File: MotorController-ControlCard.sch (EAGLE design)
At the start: 47 parts, among them J1 SL07-HORIZ, J2 SL03THROUGH_HOLE, Q7 MOSFET-PCHANNEL, Q8 MOSFET-PCHANNEL, U1 TMS320F28069MPZT, U2 MAX3232D, U3 TMS320F28069MPZT

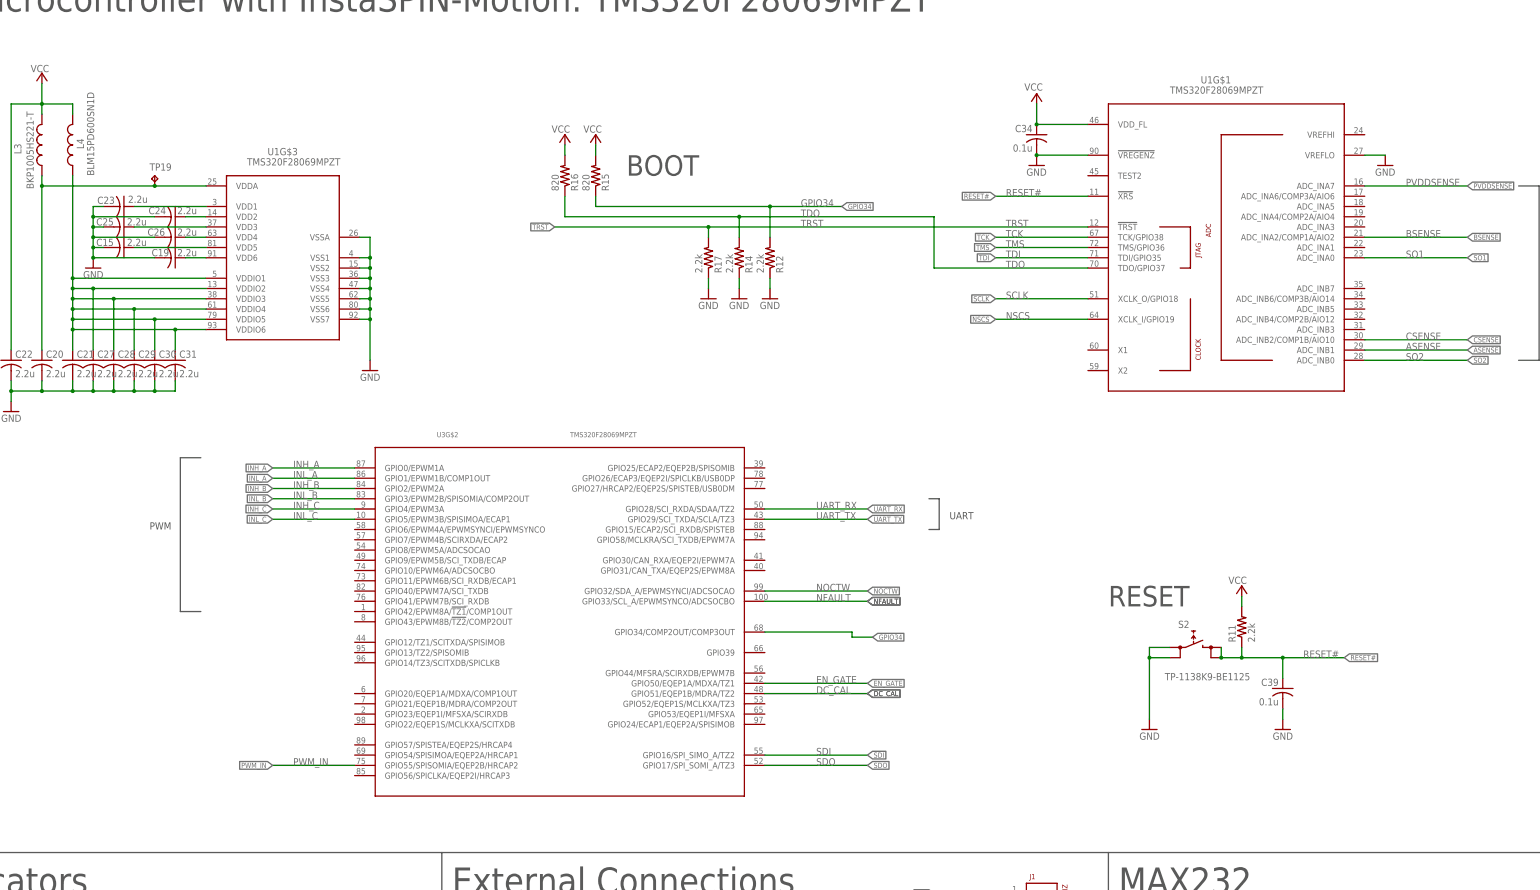
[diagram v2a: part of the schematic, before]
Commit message: Fixed Double tiva chip
Had to copy in a new set of the Tiva chip components from the Original schematic  and then I copied over all schematic routing.  New layout started due to this setback.
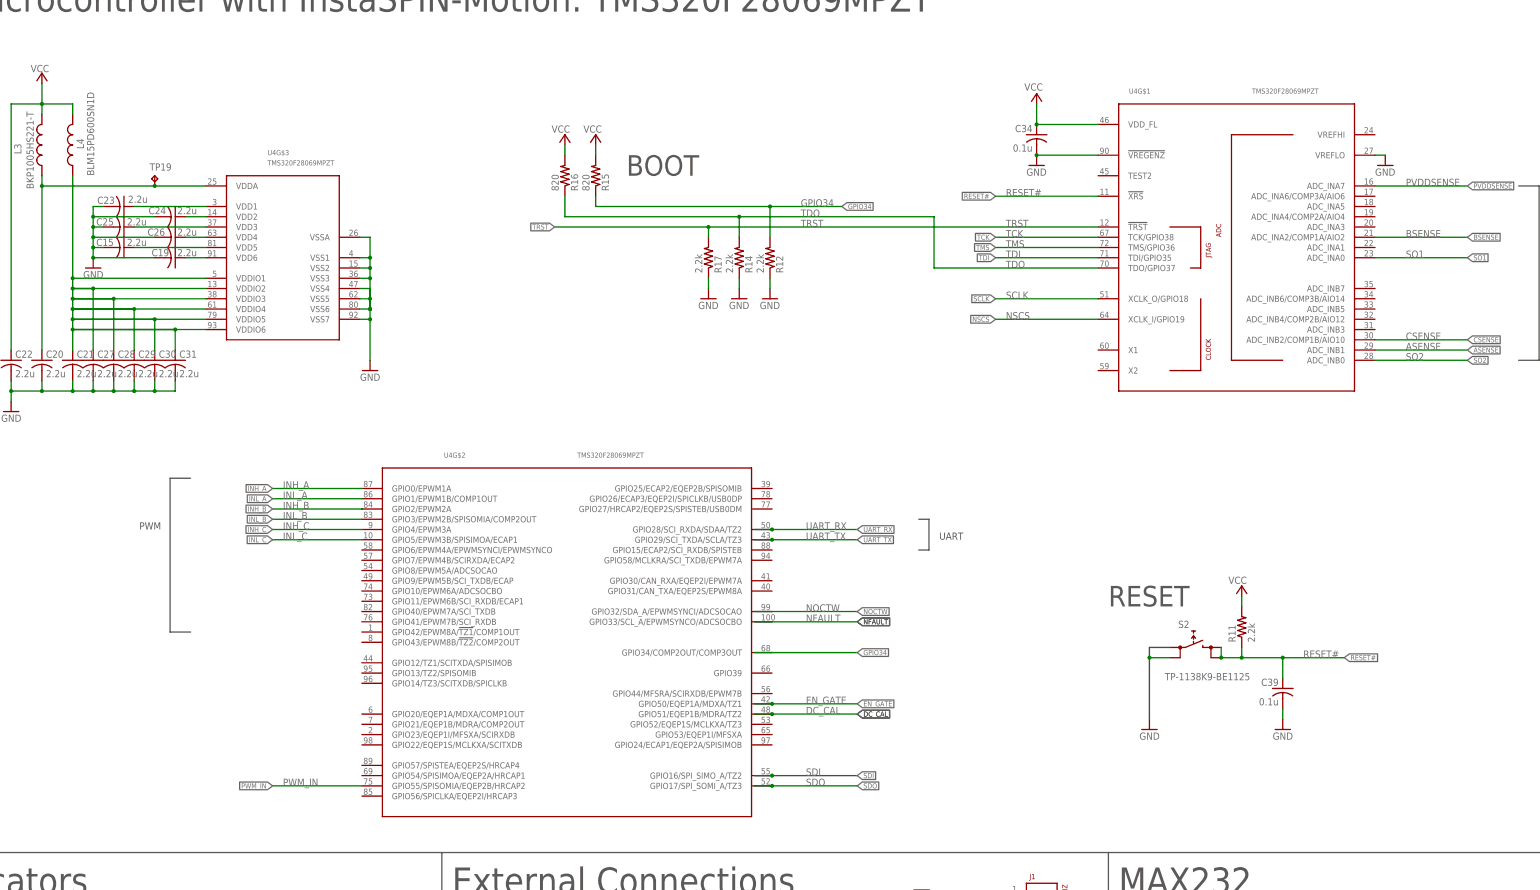
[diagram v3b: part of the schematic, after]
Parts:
- removed U1, U3: TMS320F28069MPZT, LAUNCHXL-F28027:TMS320F28069PZSR
- added U4: TMS320F28069MPZT, LAUNCHXL-F28027:TMS320F28069PZSR
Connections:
- net +3V3: now also U4G$1.VDD_FL; no longer U1G$1.VDD_FL
- net ASENSE: now also U4G$1.ADC_INB1; no longer U1G$1.ADC_INB1
- net BSENSE: now also U4G$1.ADC_INA2/COMP1A/AIO2; no longer U1G$1.ADC_INA2/COMP1A/AIO2
- net CSENSE: now also U4G$1.ADC_INB2/COMP1B/AIO10; no longer U1G$1.ADC_INB2/COMP1B/AIO10
- net DC_CAL: now also U4G$2.GPIO51/EQEP1B/MDRA/TZ2; no longer U3G$2.GPIO51/EQEP1B/MDRA/TZ2
- net EN_GATE: now also U4G$2.GPIO50/EQEP1A/MDXA/TZ1; no longer U3G$2.GPIO50/EQEP1A/MDXA/TZ1
- net GND: now also U4G$1.!VREGENZ, U4G$1.VREFLO, U4G$3.VSS1, U4G$3.VSS2, U4G$3.VSS3, U4G$3.VSS4, U4G$3.VSS5, U4G$3.VSS6, U4G$3.VSS7, U4G$3.VSSA; no longer U1G$1.!VREGENZ, U1G$1.VREFLO, U1G$3.VSS1, U1G$3.VSS2, U1G$3.VSS3, U1G$3.VSS4, U1G$3.VSS5, U1G$3.VSS6, U1G$3.VSS7, U1G$3.VSSA
- net GPIO34: now also U4G$2.GPIO34/COMP2OUT/COMP3OUT; no longer U3G$2.GPIO34/COMP2OUT/COMP3OUT
- net INH_A: now also U4G$2.GPIO0/EPWM1A; no longer U3G$2.GPIO0/EPWM1A
- net INH_B: now also U4G$2.GPIO2/EPWM2A; no longer U3G$2.GPIO2/EPWM2A
- net INH_C: now also U4G$2.GPIO4/EPWM3A; no longer U3G$2.GPIO4/EPWM3A
- net INL_A: now also U4G$2.GPIO1/EPWM1B/COMP1OUT; no longer U3G$2.GPIO1/EPWM1B/COMP1OUT
- net INL_B: now also U4G$2.GPIO3/EPWM2B/SPISOMIA/COMP2OUT; no longer U3G$2.GPIO3/EPWM2B/SPISOMIA/COMP2OUT
- net INL_C: now also U4G$2.GPIO5/EPWM3B/SPISIMOA/ECAP1; no longer U3G$2.GPIO5/EPWM3B/SPISIMOA/ECAP1
- net N$13: now also U4G$3.VDD1; no longer U1G$3.VDD1
- net N$14: now also U4G$3.VDD2; no longer U1G$3.VDD2
- net N$15: now also U4G$3.VDD3; no longer U1G$3.VDD3
- net N$16: now also U4G$3.VDD4; no longer U1G$3.VDD4
- net N$17: now also U4G$3.VDD5; no longer U1G$3.VDD5
- net N$36: now also U4G$3.VDD6; no longer U1G$3.VDD6
- net NFAULT: now also U4G$2.GPIO33/SCL_A/EPWMSYNCO/ADCSOCBO; no longer U3G$2.GPIO33/SCL_A/EPWMSYNCO/ADCSOCBO
- net NOCTW: now also U4G$2.GPIO32/SDA_A/EPWMSYNCI/ADCSOCAO; no longer U3G$2.GPIO32/SDA_A/EPWMSYNCI/ADCSOCAO
- net NSCS: now also U4G$1.XCLK_I/GPIO19; no longer U1G$1.XCLK_I/GPIO19
- net PVDDSENSE: now also U4G$1.ADC_INA7; no longer U1G$1.ADC_INA7
- net PWM_IN: now also U4G$2.GPIO55/SPISOMIA/EQEP2B/HRCAP2; no longer U3G$2.GPIO55/SPISOMIA/EQEP2B/HRCAP2
- net RESET#: now also U4G$1.!XRS; no longer U1G$1.!XRS
- net SCLK: now also U4G$1.XCLK_O/GPIO18; no longer U1G$1.XCLK_O/GPIO18
- net SDI: now also U4G$2.GPIO16/SPI_SIMO_A/TZ2; no longer U3G$2.GPIO16/SPI_SIMO_A/TZ2
- net SDO: now also U4G$2.GPIO17/SPI_SOMI_A/TZ3; no longer U3G$2.GPIO17/SPI_SOMI_A/TZ3
- net SO1: now also U4G$1.ADC_INA0; no longer U1G$1.ADC_INA0
- net SO2: now also U4G$1.ADC_INB0; no longer U1G$1.ADC_INB0
- net TCK: now also U4G$1.TCK/GPIO38; no longer U1G$1.TCK/GPIO38
- net TDI: now also U4G$1.TDI/GPIO35; no longer U1G$1.TDI/GPIO35
- net TDO: now also U4G$1.TDO/GPIO37; no longer U1G$1.TDO/GPIO37
- net TMS: now also U4G$1.TMS/GPIO36; no longer U1G$1.TMS/GPIO36
- net TRST: now also U4G$1.!TRST; no longer U1G$1.!TRST
- net UART_RX: now also U4G$2.GPIO28/SCI_RXDA/SDAA/TZ2; no longer U3G$2.GPIO28/SCI_RXDA/SDAA/TZ2
- net UART_TX: now also U4G$2.GPIO29/SCI_TXDA/SCLA/TZ3; no longer U3G$2.GPIO29/SCI_TXDA/SCLA/TZ3
- net VDDA: now also U4G$3.VDDA; no longer U1G$3.VDDA
- net VDDIO: now also U4G$3.VDDIO1, U4G$3.VDDIO2, U4G$3.VDDIO3, U4G$3.VDDIO4, U4G$3.VDDIO5, U4G$3.VDDIO6; no longer U1G$3.VDDIO1, U1G$3.VDDIO2, U1G$3.VDDIO3, U1G$3.VDDIO4, U1G$3.VDDIO5, U1G$3.VDDIO6

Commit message: Adjusted net labeling, fixed schematic organization for clarity, fixed issues detected by ERC
Adjusted External Connections section components and labeling for clarity, resolved net connection issues on the microcontroller detected by ERC, added TDO flag to boot circuit for net connection clarity, removed redundant net labeling across schematic (previously contained both flags and on-line labels)
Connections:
- removed net N$1: U$1.PA2
- removed net N$2: U$1.PA4
- removed net N$3: U$1.PA3
- removed net N$4: U$1.PA6
- removed net N$5: U$1.PA7
- removed net PWM_IN_NO_FILTER: J2.3, U$1.PF4
- net DC_CAL: now also U$1.PA3
- net EN_GATE: now also U$1.PA4
- net NFAULT: now also U$1.PA6
- net NOCTW: now also U$1.PA7
- net PWM_IN: now also J2.3, U$1.PF4, U4G$2.GPIO9/EPWM5B/SCI_TXDB/ECAP; no longer U4G$2.GPIO55/SPISOMIA/EQEP2B/HRCAP2
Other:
- note added: "Header Pins for LAUNCHXL"
- moved on the sheet: D7, D8, D9, J1, Q7, Q8, R12, R14, R16, R17, R33, R34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

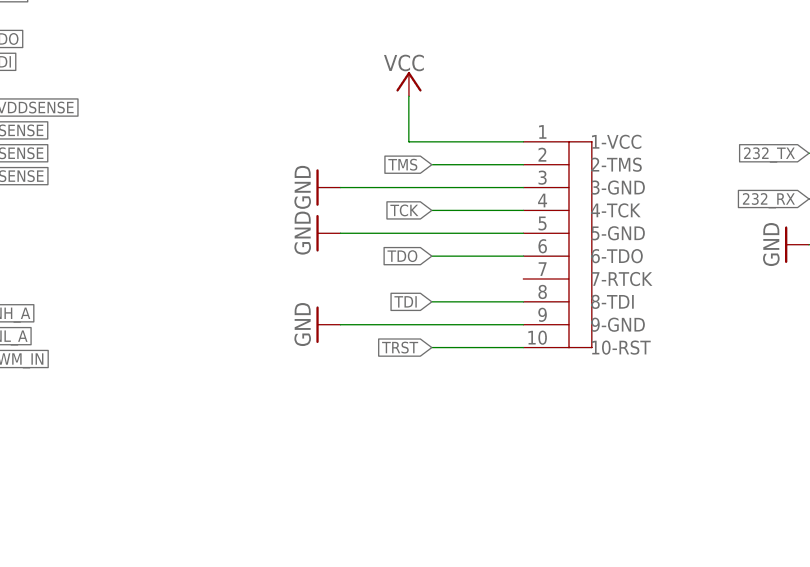
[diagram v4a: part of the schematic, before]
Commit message: Routing and Silkscreen update
SL connectors were shifted apart to better mount them. Silkcreen was added around LED's for better visibility. Board was rerouted to get the board down to two layers.
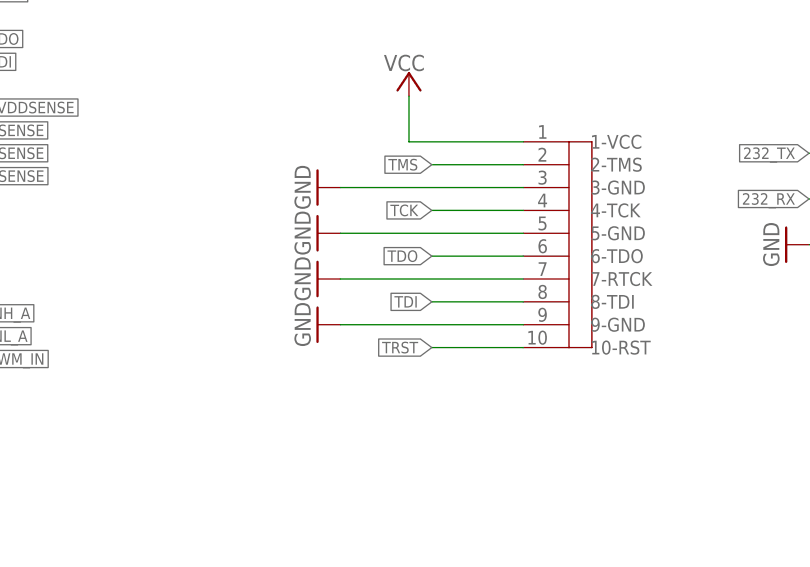
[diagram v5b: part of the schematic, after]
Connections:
- net GND: now also U$2.7-RTCK
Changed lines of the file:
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@@
 <?xml version="1.0" encoding="utf-8"?>
 <!DOCTYPE eagle SYSTEM "eagle.dtd">
-<eagle version="8.5.2">
+<eagle version="8.3.2">
 <drawing>
 <settings>
@@
 <part name="GND4" library="SparkFun-Aesthetics" deviceset="GND" device=""/>
 <part name="U4" library="LAUNCHXL-F28027" deviceset="TMS320F28069PZS" device="R" value="TMS320F28069MPZT"/>
+<part name="GND5" library="supply1" library_urn="urn:adsk.eagle:library:371" deviceset="GND" device=""/>
 </parts>
 <sheets>
@@
 </instance>
 <instance part="U4" gate="G$3" x="-35.56" y="121.92"/>
+<instance part="GND5" gate="1" x="83.82" y="-96.52" rot="R270"/>
 </instances>
 <busses>
@@
 <wire x1="35.56" y1="-113.03" x2="40.64" y2="-113.03" width="0.1524" layer="91"/>
 </segment>
+<segment>
+<pinref part="GND5" gate="1" pin="GND"/>
+<pinref part="U$2" gate="1" pin="7-RTCK"/>
+<wire x1="86.36" y1="-96.52" x2="106.68" y2="-96.52" width="0.1524" layer="91"/>
+</segment>
 </net>

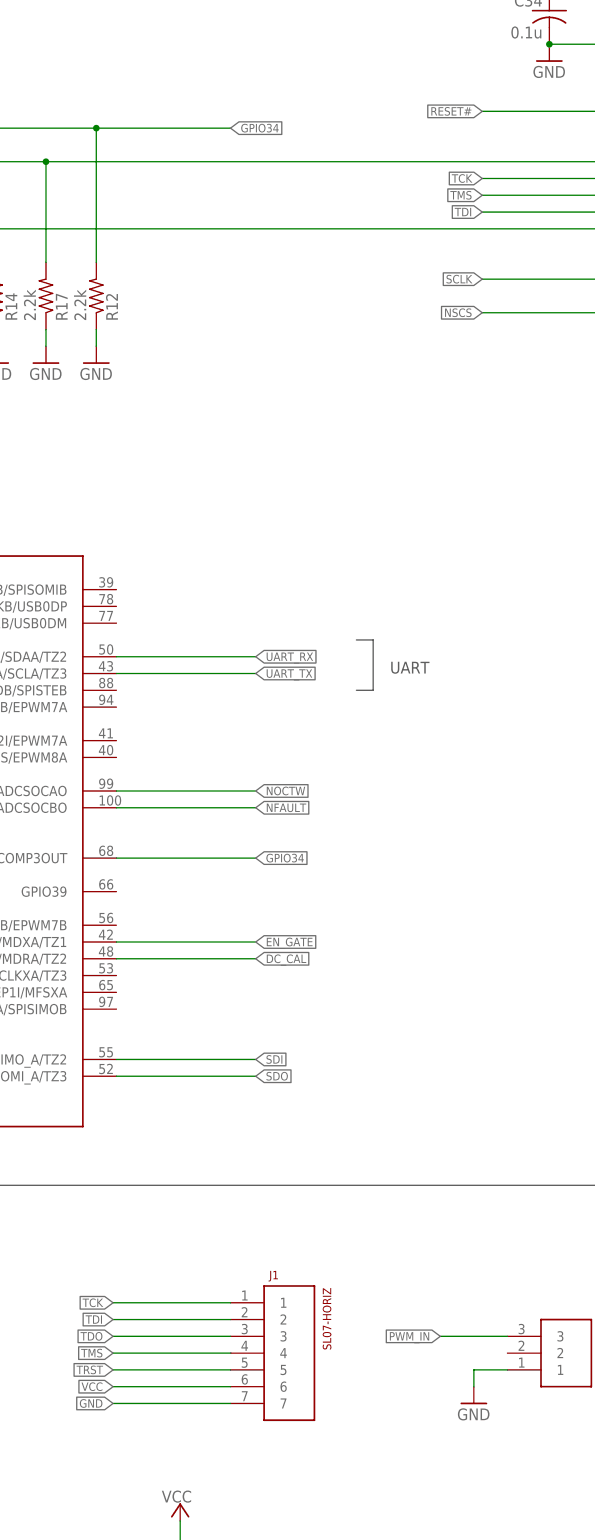
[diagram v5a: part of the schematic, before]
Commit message: Removed redundant SL connector, restructured right side of board and reduced board size
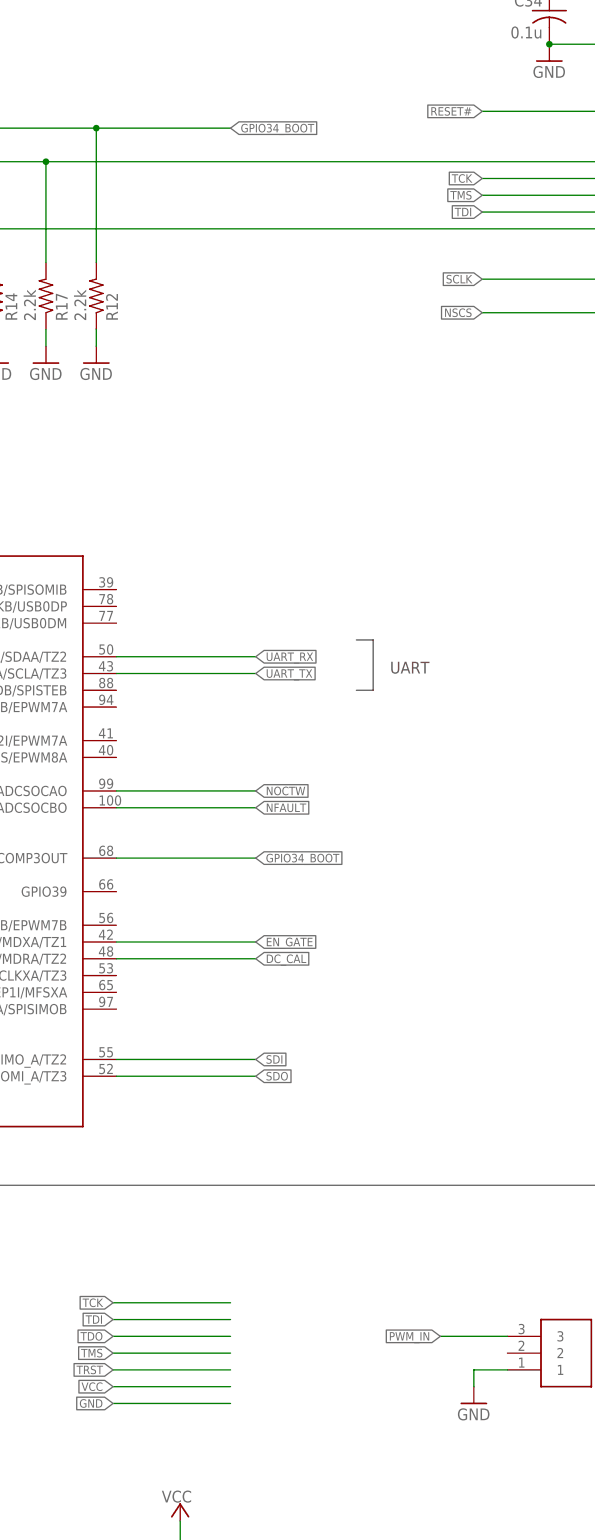
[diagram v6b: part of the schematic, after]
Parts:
- removed J1: SL07-HORIZ, MRDT-Connectors:SL07-HORIZ
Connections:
- net GPIO34 renamed GPIO34_BOOT
- net GND: no longer J1.7
- net TCK: no longer J1.1
- net TDI: no longer J1.2
- net TDO: no longer J1.3
- net TMS: no longer J1.4
- net TRST: no longer J1.5
- net VCC: no longer J1.6
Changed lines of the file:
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@@
 <part name="C39" library="rcl" deviceset="C-US" device="C0402" value="0.1u"/>
 <part name="GND39" library="supply1" library_urn="urn:adsk.eagle:library:371" deviceset="GND" device=""/>
-<part name="J1" library="MRDT-Connectors" deviceset="SL07" device="-HORIZ"/>
 <part name="R12" library="rcl" deviceset="R-US_" device="R0402" value="2.2k"/>
 <part name="R14" library="rcl" deviceset="R-US_" device="R0402" value="2.2k"/>
@@
 <instance part="C39" gate="G$1" x="210.82" y="15.24" rot="MR0"/>
 <instance part="GND39" gate="1" x="210.82" y="5.08" rot="MR0"/>
-<instance part="J1" gate="G$1" x="114.3" y="-40.64" rot="R270"/>
 <instance part="R12" gate="G$1" x="81.28" y="109.22" rot="MR90"/>
 <instance part="R14" gate="G$1" x="66.04" y="109.22" rot="MR90"/>
@@
 </segment>
 <segment>
-<pinref part="J1" gate="G$1" pin="7"/>
 <wire x1="101.6" y1="-58.42" x2="83.82" y2="-58.42" width="0.1524" layer="91"/>
 <label x="83.82" y="-58.42" size="1.27" layer="95" rot="R180" xref="yes"/>
@@
 </segment>
 <segment>
-<pinref part="J1" gate="G$1" pin="6"/>
 <wire x1="101.6" y1="-55.88" x2="83.82" y2="-55.88" width="0.1524" layer="91"/>
 <label x="83.82" y="-55.88" size="1.27" layer="95" rot="R180" xref="yes"/>
@@
 </segment>
 </net>
-<net name="GPIO34" class="0">
+<net name="GPIO34_BOOT" class="0">
 <segment>
 <wire x1="81.28" y1="134.62" x2="81.28" y2="114.3" width="0.1524" layer="91"/>
@@
 </segment>
 <segment>
-<pinref part="J1" gate="G$1" pin="1"/>
 <wire x1="101.6" y1="-43.18" x2="83.82" y2="-43.18" width="0.1524" layer="91"/>
 <label x="83.82" y="-43.18" size="1.27" layer="95" rot="R180" xref="yes"/>
@@
 </segment>
 <segment>
-<pinref part="J1" gate="G$1" pin="2"/>
 <wire x1="101.6" y1="-45.72" x2="83.82" y2="-45.72" width="0.1524" layer="91"/>
 <label x="83.82" y="-45.72" size="1.27" layer="95" rot="R180" xref="yes"/>
@@
 <net name="TDO" class="0">
 <segment>
-<pinref part="J1" gate="G$1" pin="3"/>
 <wire x1="101.6" y1="-48.26" x2="83.82" y2="-48.26" width="0.1524" layer="91"/>
 <label x="83.82" y="-48.26" size="1.27" layer="95" rot="R180" xref="yes"/>
@@
 </segment>
 <segment>
-<pinref part="J1" gate="G$1" pin="4"/>
 <wire x1="101.6" y1="-50.8" x2="83.82" y2="-50.8" width="0.1524" layer="91"/>
 <label x="83.82" y="-50.8" size="1.27" layer="95" rot="R180" xref="yes"/>
@@
 <net name="TRST" class="0">
 <segment>
-<pinref part="J1" gate="G$1" pin="5"/>
 <wire x1="101.6" y1="-53.34" x2="83.82" y2="-53.34" width="0.1524" layer="91"/>
 <label x="83.82" y="-53.34" size="1.27" layer="95" rot="R180" xref="yes"/>
